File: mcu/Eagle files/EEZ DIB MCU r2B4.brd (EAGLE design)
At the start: 139.5 x 70 mm, 184 parts, among them IC1 TPD4E001DRLR, IC10 TPD4E001DRLR, IC11 N.C., IC12 TSC2007IPW, IC13 N.C., IC14 DP83848CVV/NOPB, IC2 CD74HC4050PWR, IC3 STM32F769IGT6, IC4 LD1117ADT33TR, IC5 N.C., IC6 IS42S16400J, IC7 AT24C256C-SSHL-B, IC8 TPS2051BDBVR, IC9 TPS61169DCKR, J1 503398-1892, J2 67803-8020, Q1 N.C., Q2 2N7002, SW1 TL1100CF160Q, SW2 PEC16-2215F-S0024, SW3 EVQP7A01P, X1 DS1024-2*20R0, X2 DS1013-16SSIB1, X3 691322110005, X4 N.C., X5 LMJTAB881243M-L, Y1 25MHz, Y2 XTAL016178-85SMX

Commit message: MCU part number updated in schematics
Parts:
- IC3: value STM32F769IGT6 -> STM32F769IIT6
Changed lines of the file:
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@@
 <attribute name="VALUE" x="102.9335" y="16.637" size="1.016" layer="27" ratio="10" rot="R90"/>
 </element>
-<element name="IC3" library="EEZ_DIB" package="LQFP-176_24X24MM" value="STM32F769IGT6" x="69.5325" y="46.2915" locked="yes" smashed="yes" rot="R315">
+<element name="IC3" library="EEZ_DIB" package="LQFP-176_24X24MM" value="STM32F769IIT6" x="69.5325" y="46.2915" locked="yes" smashed="yes" rot="R315">
 <attribute name="COPYRIGHT" value="Copyright C 2016 Accelerated Designs. All rights reserved" x="69.5325" y="46.2915" size="1.778" layer="27" rot="R315" display="off"/>
 <attribute name="MANUFACTURER_PART_NUMBER" value="stm32f769ixt" x="69.5325" y="46.2915" size="1.778" layer="27" rot="R315" display="off"/>

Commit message: MCU ZD1 value correction
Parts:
- ZD1: value BZX384-B30.115 -> BZX384-B24.115
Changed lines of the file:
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@@
 <attribute name="VALUE" x="67.1957" y="20.0406" size="1.016" layer="27" ratio="10"/>
 </element>
-<element name="ZD1" library="EEZ_Lib1" package="SOD323-W" value="BZX384-B30.115" x="42.3545" y="13.8811" smashed="yes" rot="R90">
+<element name="ZD1" library="EEZ_Lib1" package="SOD323-W" value="BZX384-B24.115" x="42.3545" y="13.8811" smashed="yes" rot="R90">
 <attribute name="NAME" x="41.6003" y="14.9131" size="0.8128" layer="25" ratio="10" rot="R180"/>
 <attribute name="VALUE" x="42.7368" y="9.2632" size="0.6096" layer="27" ratio="10" rot="R90"/>

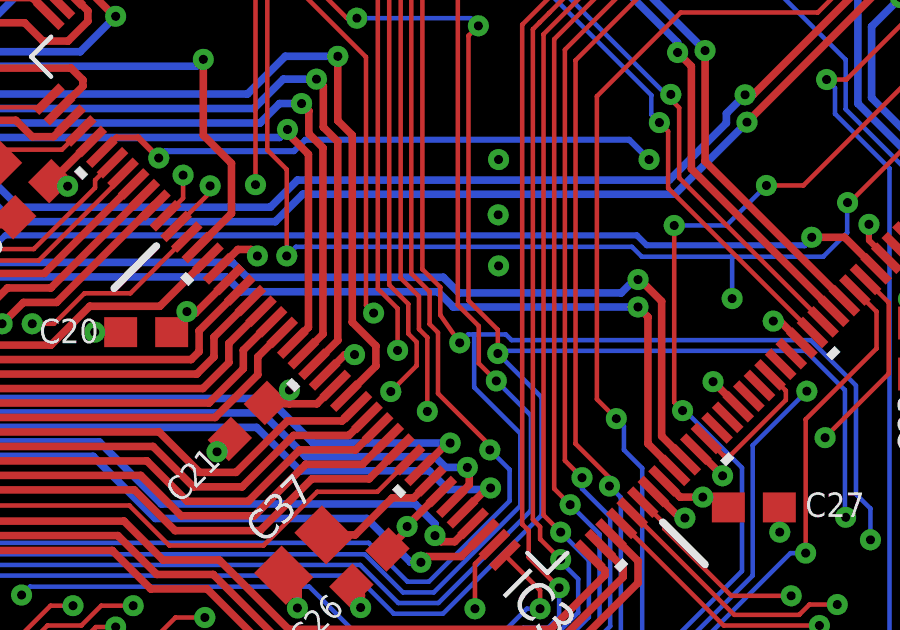
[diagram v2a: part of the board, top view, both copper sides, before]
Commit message: MCU I2C pull-up update
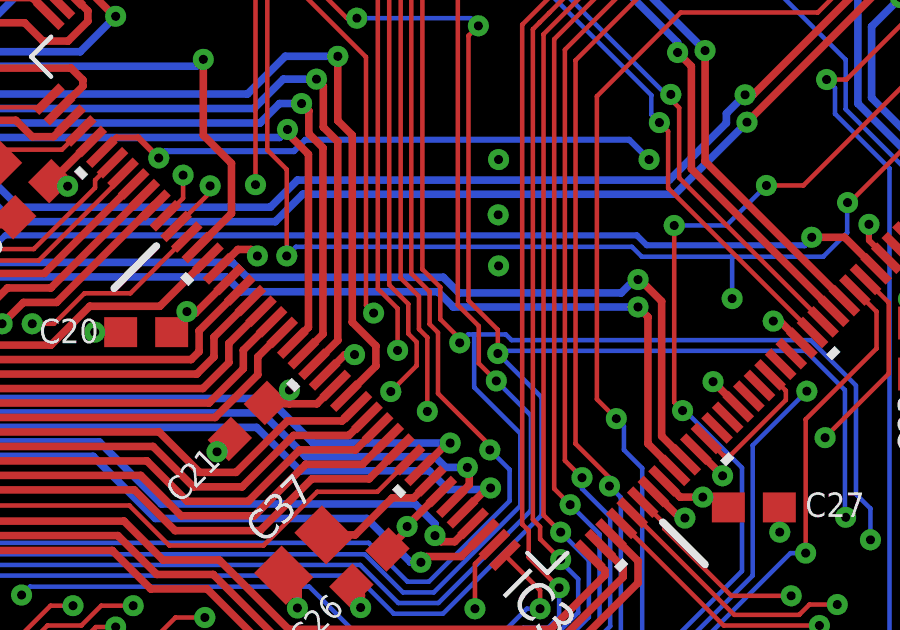
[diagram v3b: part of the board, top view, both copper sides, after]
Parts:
- C8: value 1n -> N.C.
- R15, R16: value 4K7 -> 2K2
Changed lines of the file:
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@@
 <grid distance="2.5" unitdist="mil" unit="mil" style="lines" multiple="10" display="no" altdistance="12.5" altunitdist="mil" altunit="mil"/>
 <layers>
-<layer number="1" name="Top" color="11" fill="1" visible="yes" active="yes"/>
+<layer number="1" name="Top" color="11" fill="1" visible="no" active="yes"/>
 <layer number="2" name="Gnd" color="2" fill="1" visible="no" active="yes"/>
 <layer number="3" name="Route3" color="4" fill="3" visible="no" active="no"/>
@@
 <layer number="14" name="Route14" color="1" fill="6" visible="no" active="no"/>
 <layer number="15" name="Power" color="6" fill="1" visible="no" active="yes"/>
-<layer number="16" name="Bottom" color="1" fill="1" visible="yes" active="yes"/>
-<layer number="17" name="Pads" color="6" fill="1" visible="yes" active="yes"/>
-<layer number="18" name="Vias" color="6" fill="1" visible="yes" active="yes"/>
+<layer number="16" name="Bottom" color="1" fill="1" visible="no" active="yes"/>
+<layer number="17" name="Pads" color="6" fill="1" visible="no" active="yes"/>
+<layer number="18" name="Vias" color="6" fill="1" visible="no" active="yes"/>
 <layer number="19" name="Unrouted" color="6" fill="1" visible="no" active="yes"/>
 <layer number="20" name="Dimension" color="12" fill="1" visible="yes" active="yes"/>
 <layer number="21" name="tPlace" color="7" fill="1" visible="yes" active="yes"/>
-<layer number="22" name="bPlace" color="13" fill="1" visible="yes" active="yes"/>
+<layer number="22" name="bPlace" color="13" fill="1" visible="no" active="yes"/>
 <layer number="23" name="tOrigins" color="15" fill="1" visible="no" active="yes"/>
-<layer number="24" name="bOrigins" color="15" fill="1" visible="yes" active="yes"/>
+<layer number="24" name="bOrigins" color="15" fill="1" visible="no" active="yes"/>
 <layer number="25" name="tNames" color="7" fill="1" visible="yes" active="yes"/>
-<layer number="26" name="bNames" color="13" fill="1" visible="yes" active="yes"/>
-<layer number="27" name="tValues" color="10" fill="1" visible="no" active="yes"/>
+<layer number="26" name="bNames" color="13" fill="1" visible="no" active="yes"/>
+<layer number="27" name="tValues" color="10" fill="1" visible="yes" active="yes"/>
 <layer number="28" name="bValues" color="11" fill="1" visible="no" active="yes"/>
-<layer number="29" name="tStop" color="15" fill="1" visible="no" active="yes"/>
+<layer number="29" name="tStop" color="15" fill="1" visible="yes" active="yes"/>
 <layer number="30" name="bStop" color="7" fill="6" visible="no" active="yes"/>
 <layer number="31" name="tCream" color="7" fill="4" visible="no" active="yes"/>
@@
 <layer number="37" name="tTest" color="7" fill="1" visible="no" active="yes"/>
 <layer number="38" name="bTest" color="7" fill="1" visible="no" active="yes"/>
-<layer number="39" name="tKeepout" color="15" fill="1" visible="no" active="yes"/>
+<layer number="39" name="tKeepout" color="15" fill="1" visible="yes" active="yes"/>
 <layer number="40" name="bKeepout" color="13" fill="1" visible="no" active="yes"/>
 <layer number="41" name="tRestrict" color="4" fill="10" visible="no" active="yes"/>
@@
 <attribute name="VALUE" x="88.9762" y="6.5659" size="1.016" layer="27" ratio="10"/>
 </element>
-<element name="R16" library="rcl" package="R0805" value="4K7" x="78.0542" y="62.738" smashed="yes" rot="R270">
+<element name="R16" library="rcl" package="R0805" value="2K2" x="78.0542" y="62.738" smashed="yes" rot="R270">
 <attribute name="NAME" x="77.0509" y="64.8716" size="0.8128" layer="25" ratio="10"/>
 <attribute name="VALUE" x="78.5368" y="61.468" size="1.016" layer="27" ratio="10" rot="R90"/>
 </element>
-<element name="R15" library="rcl" package="R0805" value="4K7" x="80.0227" y="62.738" smashed="yes" rot="R270">
+<element name="R15" library="rcl" package="R0805" value="2K2" x="80.0227" y="62.738" smashed="yes" rot="R270">
 <attribute name="NAME" x="79.248" y="64.8843" size="0.8128" layer="25" ratio="10"/>
 <attribute name="VALUE" x="80.5053" y="61.4045" size="1.016" layer="27" ratio="10" rot="R90"/>
@@
 <attribute name="VALUE" x="34.0106" y="14.8463" size="0.8128" layer="27" ratio="10" rot="R180"/>
 </element>
-<element name="C8" library="rcl" package="C0805" value="1n" x="52.9082" y="54.0639" smashed="yes" rot="R180">
+<element name="C8" library="rcl" package="C0805" value="N.C." x="52.9082" y="54.0639" smashed="yes" rot="R180">
 <attribute name="NAME" x="55.0164" y="53.6829" size="1.016" layer="25" ratio="10"/>
-<attribute name="VALUE" x="53.8099" y="54.5846" size="1.016" layer="27" ratio="10" rot="R180"/>
+<attribute name="VALUE" x="51.7271" y="53.5559" size="1.016" layer="27" ratio="10"/>
 </element>
 <element name="SW3" library="EEZ_switches" package="PANASONIC_EVQP" value="EVQP7A01P" x="21" y="3" smashed="yes" rot="R180">
@@
 <wire x1="65.3669" y1="53.7591" x2="65.659" y2="54.0512" width="0.1524" layer="1"/>
 <wire x1="65.3669" y1="39.2049" x2="65.9638" y2="38.608" width="0.1524" layer="1"/>
-<wire x1="65.9638" y1="38.608" x2="65.9638" y2="37.6809" width="0.1524" layer="1"/>
-<wire x1="65.9638" y1="37.6809" x2="66.6115" y2="36.7538" width="0.1524" layer="1"/>
+<wire x1="65.9638" y1="38.608" x2="65.9638" y2="37.5412" width="0.1524" layer="1"/>
 <wire x1="68.1482" y1="37.0332" x2="68.3387" y2="36.8427" width="0.1524" layer="16"/>
 <wire x1="94.0689" y1="30.1879" x2="80.3021" y2="30.1879" width="0.1524" layer="15"/>
@@
 <wire x1="36.4744" y1="28.4734" x2="35.3568" y2="28.4734" width="0.1524" layer="16"/>
 <wire x1="35.3568" y1="28.4734" x2="34.9758" y2="28.8544" width="0.1524" layer="16"/>
+<wire x1="66.6115" y1="36.7538" x2="66.6115" y2="36.8935" width="0.1524" layer="1"/>
+<wire x1="66.6115" y1="36.8935" x2="65.9638" y2="37.5412" width="0.1524" layer="1"/>
 </signal>
 <signal name="DOUT2">

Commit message: MCU IC6 model type update
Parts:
- IC6: value IS42S16400J -> IS42S16400J-7TL
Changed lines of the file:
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@@
 <attribute name="VALUE" x="10.09524375" y="32.78111875" size="0.6096" layer="27" ratio="10"/>
 </element>
-<element name="IC6" library="EEZ_Lib1" package="TSOPII-54" value="IS42S16400J" x="34.0995" y="47.6885" smashed="yes" rot="R180">
+<element name="IC6" library="EEZ_Lib1" package="TSOPII-54" value="IS42S16400J-7TL" x="34.0995" y="47.6885" smashed="yes" rot="R180">
 <attribute name="NAME" x="32.7279" y="34.9123" size="1.27" layer="25" ratio="10"/>
 <attribute name="VALUE" x="33.528" y="53.6575" size="1.016" layer="27" ratio="10" rot="R270"/>
